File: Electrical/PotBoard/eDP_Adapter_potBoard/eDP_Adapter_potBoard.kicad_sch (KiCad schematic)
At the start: 6 parts, among them J1 Conn_01x05, M1 Standoff, M2 Standoff, M3 Standoff, U2 PotBoard

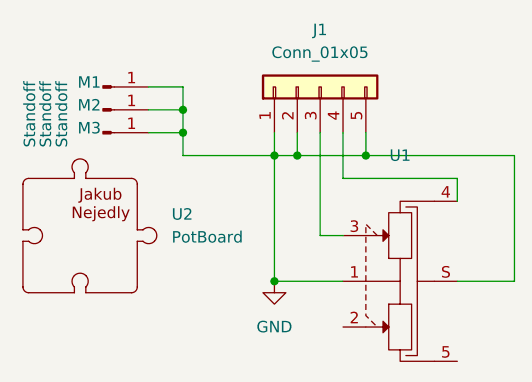
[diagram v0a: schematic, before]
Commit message: BOM and fixed potboard font
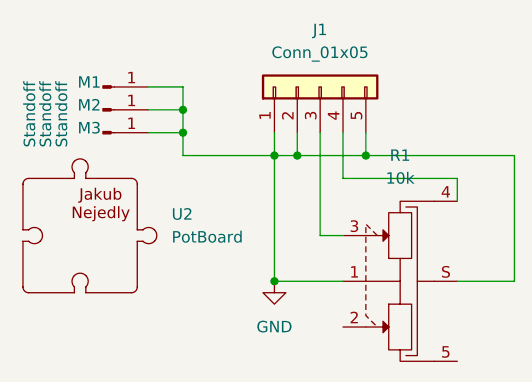
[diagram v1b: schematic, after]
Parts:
- R1: renamed from U1; value ~ -> 10k
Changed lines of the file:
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@@
 		(on_board yes)
 		(dnp no)
-		(property "Reference" "U1"
+		(property "Reference" "R1"
 			(at 57.15 30.48 0)
 			(effects
@@
 			)
 		)
-		(property "Value" "~"
+		(property "Value" "10k"
 			(at 57.15 33.02 0)
 			(effects
@@
 			(project ""
 				(path "/7af0dfd6-81ff-472f-9c57-2b485db774fa"
-					(reference "U1")
+					(reference "R1")
 					(unit 1)
 				)
